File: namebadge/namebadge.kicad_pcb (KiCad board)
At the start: 2 copper layers, 77 x 24 mm, 2 parts

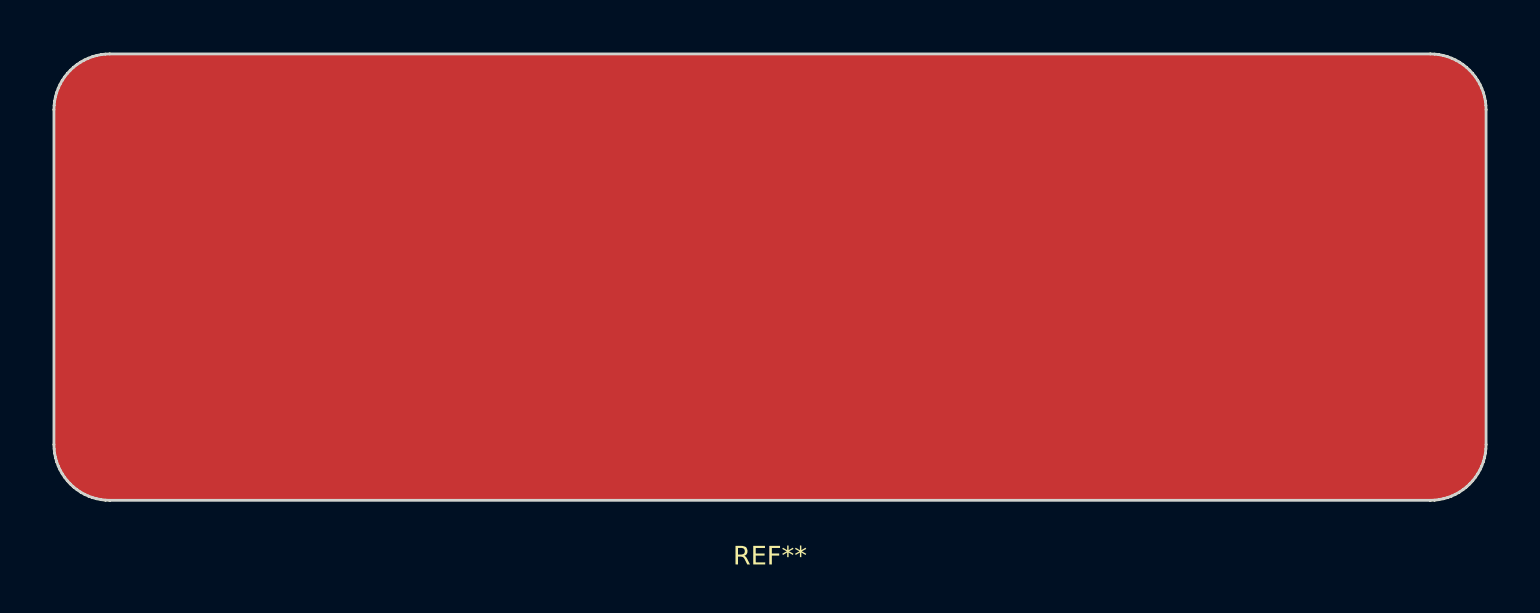
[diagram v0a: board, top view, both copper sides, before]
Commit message: Namebadge in black/white.
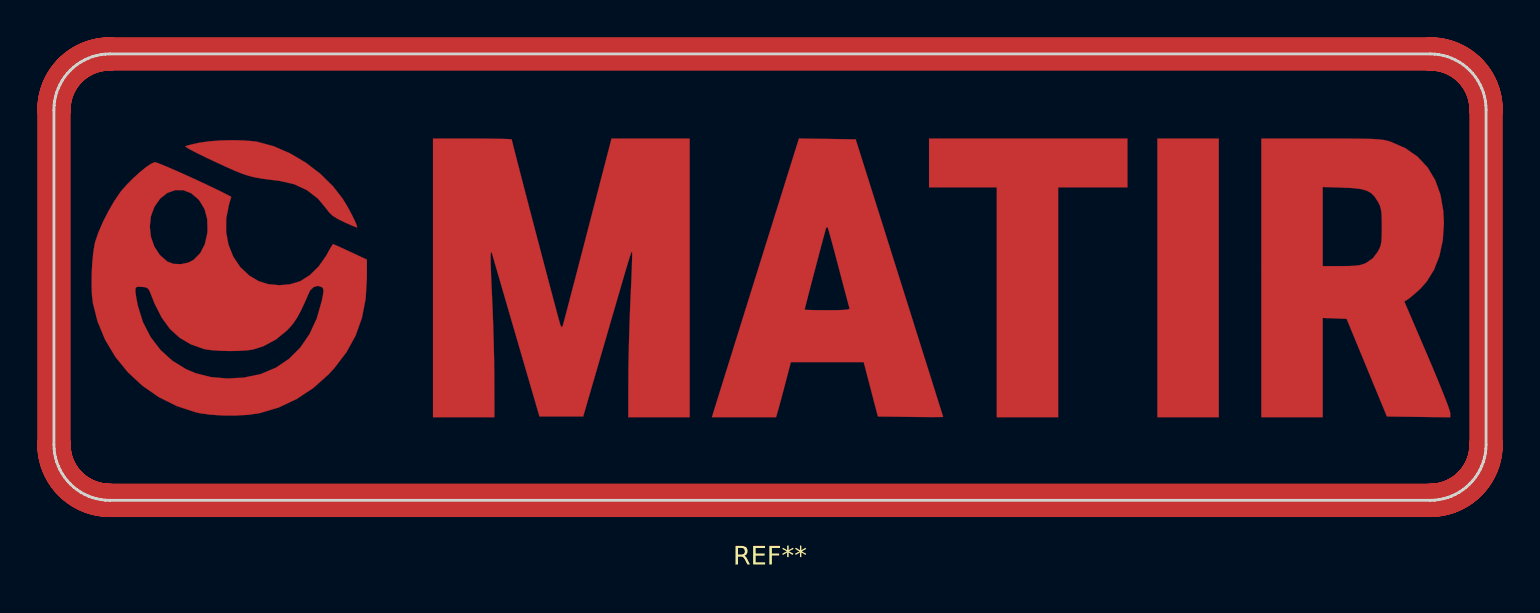
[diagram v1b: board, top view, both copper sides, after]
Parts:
- G***: footprint badge:name -> badge:name_cu
- REF**: footprint badge:border -> badge:border_empty
